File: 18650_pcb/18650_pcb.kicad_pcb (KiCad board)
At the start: 2 copper layers, 40 x 88 mm, 3 parts, among them P1 CONN_01X02

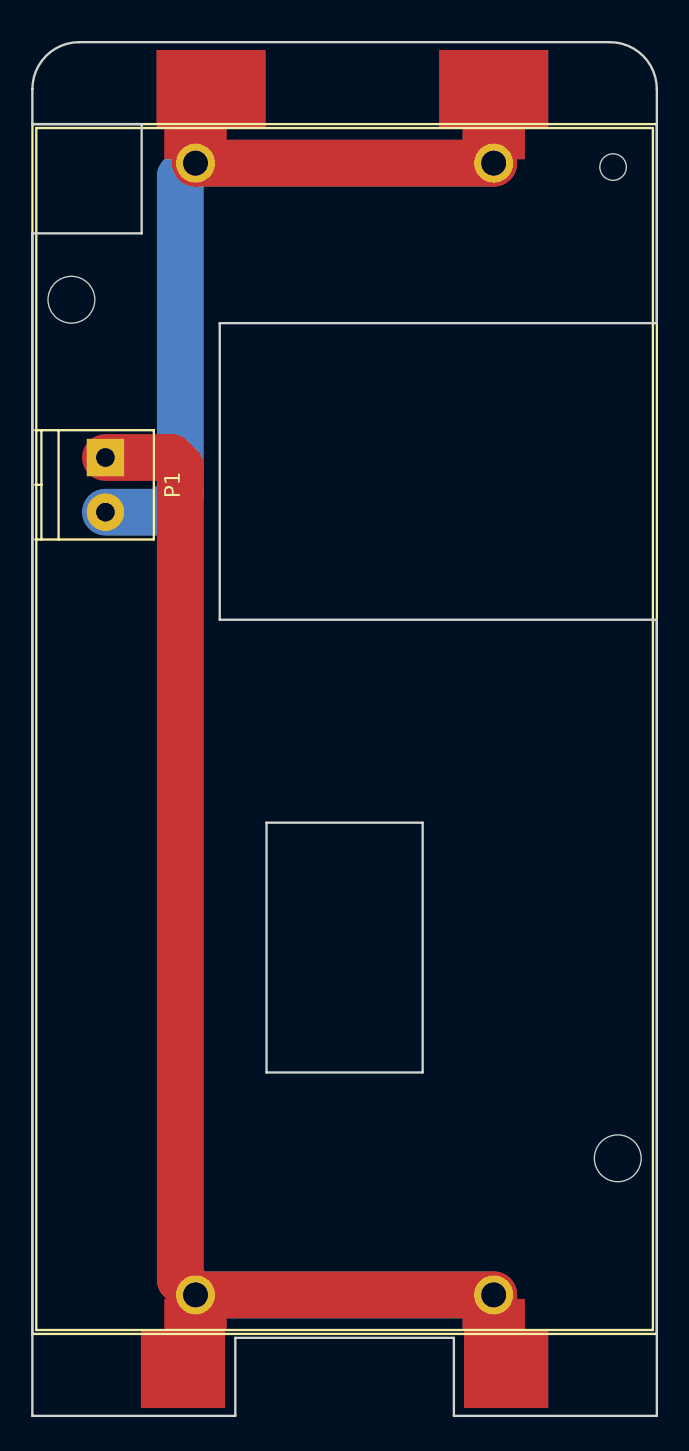
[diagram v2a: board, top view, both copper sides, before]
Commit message: 18650 PCB modifications
-Added version information
-Added a fuse between two batteries
-Added polarity silkscreen markings
-Removed traces from bottom layer to prevent them from shorting out to
metal on back PCB
-Added pads for hand-soldering JST connector wires onto the board
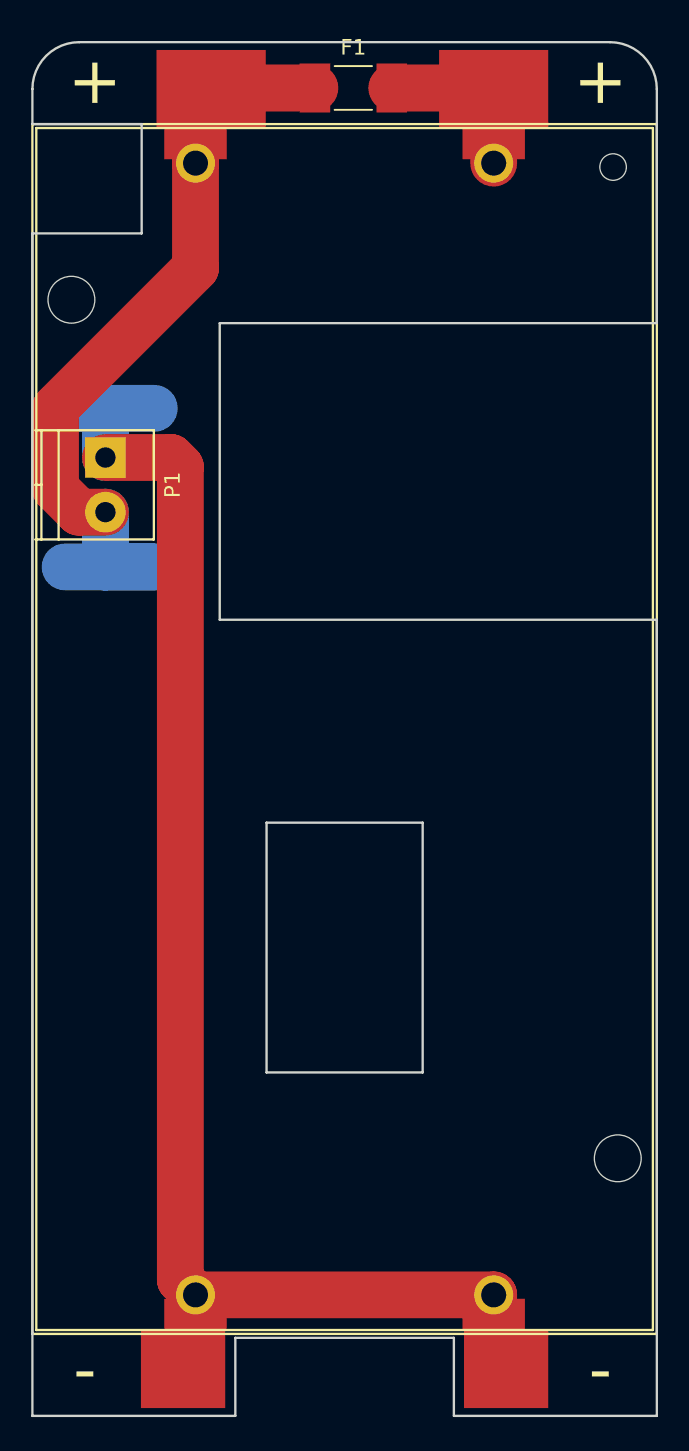
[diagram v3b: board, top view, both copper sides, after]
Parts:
- added F1: 1A, Fuse_Holders_and_Fuses:Fuse_0679H, F.Cu at (150.6, 58.9)
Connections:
- BT1 pad 2: Net-(BT1-Pad1) -> Net-(BT1-Pad2)
- BT2 pad 2: Net-(BT1-Pad1) -> Net-(BT1-Pad2)
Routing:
- net Net-(BT1-Pad1): track 74.7 -> 52.2 mm
- net Net-(BT1-Pad2): track 0.00 -> 11.3 mm
- net Net-(BT1-Pad3): track 106.2 -> 98.5 mm
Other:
- board text added: "+"
- board text added: "-"
- board text added: "18650 PCB ZeroPhone Delta"
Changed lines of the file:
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@@
-(kicad_pcb (version 4) (host pcbnew 4.0.4-stable)
+(kicad_pcb (version 4) (host pcbnew 4.0.6)
   (general
-    (links 12)
-    (no_connects 0)
+    (links 13)
+    (no_connects 2)
     (area 129.924999 55.924999 170.075001 144.075001)
     (thickness 1.6)
-    (drawings 22)
-    (tracks 17)
+    (drawings 28)
+    (tracks 26)
     (zones 0)
-    (modules 3)
-    (nets 3)
+    (modules 4)
+    (nets 4)
   )
   (page A4)
@@
     (mod_text_size 1 1)
     (mod_text_width 0.15)
-    (pad_size 7 5)
-    (pad_drill 0)
+    (pad_size 2.6 2.6)
+    (pad_drill 1.3)
     (pad_to_mask_clearance 0.2)
-    (aux_axis_origin 0 0)
-    (grid_origin 148.57862 104.90804)
-    (visible_elements 7FFFFFFF)
+    (aux_axis_origin 172.09902 54.05724)
+    (grid_origin 172.09902 54.05724)
+    (visible_elements 7FFFFF7F)
     (pcbplotparams
       (layerselection 0x010f0_80000001)
@@
   (net 1 "Net-(BT1-Pad1)")
   (net 2 "Net-(BT1-Pad3)")
+  (net 3 "Net-(BT1-Pad2)")
   (net_class Default "This is the default net class."
     (clearance 0.2)
@@
     (uvia_drill 0.1)
     (add_net "Net-(BT1-Pad1)")
+    (add_net "Net-(BT1-Pad2)")
     (add_net "Net-(BT1-Pad3)")
   )
@@
       (effects (font (size 1 1) (thickness 0.15)))
     )
-    (fp_text value 2x_Battery_Holder (at -0.12138 -27.49196) (layer B.Fab)
+    (fp_text value 2x_Battery_Holder (at -0.12138 -27.49196) (layer B.Fab) hide
       (effects (font (size 1 1) (thickness 0.15)) (justify mirror))
     )
@@
       (net 1 "Net-(BT1-Pad1)"))
     (pad 2 thru_hole circle (at 9.55 -36.25) (size 2.5 2.5) (drill 1.6) (layers *.Cu *.Mask)
-      (net 1 "Net-(BT1-Pad1)"))
+      (net 3 "Net-(BT1-Pad2)"))
     (pad 3 thru_hole circle (at -9.55 36.25) (size 2.5 2.5) (drill 1.6) (layers *.Cu *.Mask)
       (net 2 "Net-(BT1-Pad3)"))
@@
       (effects (font (size 1 1) (thickness 0.15)))
     )
-    (fp_text value 2x_Battery_Holder (at 0.37862 -29.59196 180) (layer F.Fab)
+    (fp_text value 2x_Battery_Holder (at 0.37862 -29.59196) (layer F.Fab) hide
       (effects (font (size 1 1) (thickness 0.15)))
     )
@@
       (net 1 "Net-(BT1-Pad1)"))
     (pad 2 smd rect (at 9.55 -41) (size 7 5) (layers F.Cu F.Paste F.Mask)
-      (net 1 "Net-(BT1-Pad1)"))
+      (net 3 "Net-(BT1-Pad2)"))
     (pad 3 smd rect (at -10.35 41) (size 5.4 5) (layers F.Cu F.Paste F.Mask)
       (net 2 "Net-(BT1-Pad3)"))
@@
       (net 1 "Net-(BT1-Pad1)"))
     (pad 2 smd rect (at 9.55 -37.5) (size 4 2) (layers F.Cu F.Paste F.Mask)
-      (net 1 "Net-(BT1-Pad1)"))
+      (net 3 "Net-(BT1-Pad2)"))
     (pad 3 smd rect (at -9.55 37.5) (size 4 2) (layers F.Cu F.Paste F.Mask)
       (net 2 "Net-(BT1-Pad3)"))
@@
     (fp_line (start 5.25 4.5) (end 5.25 -3.1) (layer F.SilkS) (width 0.15))
     (fp_line (start 5.25 -3.1) (end -1.75 -3.1) (layer F.SilkS) (width 0.15))
-    (pad 2 thru_hole circle (at 3.5 0 270) (size 2.4 2.4) (drill 1.2) (layers *.Cu *.Mask)
-      (net 1 "Net-(BT1-Pad1)"))
-    (pad 1 thru_hole rect (at 0 0 270) (size 2.4 2.4) (drill 1.2) (layers *.Cu *.Mask)
-      (net 2 "Net-(BT1-Pad3)"))
-    (model Terminal_Blocks.3dshapes/TerminalBlock_Pheonix_PT-3.5mm_2pol.wrl
-      (at (xyz 0 0 0))
-      (scale (xyz 1 1 1))
-      (rotate (xyz 0 0 0))
-    )
-  )
+    (pad 2 thru_hole circle (at 3.5 0 270) (size 2.6 2.6) (drill 1.3) (layers *.Cu *.Mask)
+      (net 1 "Net-(BT1-Pad1)"))
+    (pad 1 thru_hole rect (at 0 0 270) (size 2.6 2.6) (drill 1.3) (layers *.Cu *.Mask)
+      (net 2 "Net-(BT1-Pad3)"))
+  )
+  (module Fuse_Holders_and_Fuses:Fuse_0679H (layer F.Cu)
+    (at 150.55982 58.93404)
+    (descr "0679H Series, 2410 Size")
+    (tags Fuse)
+    (attr smd)
+    (fp_text reference F1 (at 0 -2.6) (layer F.SilkS)
+      (effects (font (size 1 1) (thickness 0.15)))
+    )
+    (fp_text value 1A (at 0 2.6) (layer F.Fab)
+      (effects (font (size 1 1) (thickness 0.15)))
+    )
+    (fp_line (start -3.7 1.85) (end -3.7 -1.85) (layer F.CrtYd) (width 0.05))
+    (fp_line (start 3.7 1.85) (end -3.7 1.85) (layer F.CrtYd) (width 0.05))
+    (fp_line (start 3.7 -1.85) (end 3.7 1.85) (layer F.CrtYd) (width 0.05))
+    (fp_line (start -3.7 -1.85) (end 3.7 -1.85) (layer F.CrtYd) (width 0.05))
+    (fp_line (start -1.2 1.4) (end 1.2 1.4) (layer F.SilkS) (width 0.12))
+    (fp_line (start -1.2 -1.4) (end 1.2 -1.4) (layer F.SilkS) (width 0.12))
+    (fp_line (start -3.05 1.27) (end -3.05 -1.27) (layer F.Fab) (width 0.1))
+    (fp_line (start 3.05 1.27) (end -3.05 1.27) (layer F.Fab) (width 0.1))
+    (fp_line (start 3.05 -1.27) (end 3.05 1.27) (layer F.Fab) (width 0.1))
+    (fp_line (start -3.05 -1.27) (end 3.05 -1.27) (layer F.Fab) (width 0.1))
+    (pad 2 smd rect (at 2.46 0) (size 1.96 3.15) (layers F.Cu F.Paste F.Mask)
+      (net 3 "Net-(BT1-Pad2)"))
+    (pad 1 smd rect (at -2.46 0) (size 1.96 3.15) (layers F.Cu F.Paste F.Mask)
+      (net 1 "Net-(BT1-Pad1)"))
+  )
+  (gr_text - (at 166.38402 141.05224) (layer F.SilkS)
+    (effects (font (size 3 3) (thickness 0.6)))
+  )
+  (gr_text - (at 133.36402 141.05224) (layer F.SilkS)
+    (effects (font (size 3 3) (thickness 0.6)))
+  )
+  (gr_text + (at 166.38402 58.50224) (layer F.SilkS)
+    (effects (font (size 3 3) (thickness 0.6)))
+  )
+  (gr_text + (at 133.99902 58.50224) (layer F.SilkS)
+    (effects (font (size 3 3) (thickness 0.6)))
+  )
+  (gr_text "18650 PCB\nZeroPhone Delta" (at 149.87402 68.66224) (layer B.SilkS)
+    (effects (font (size 2 2) (thickness 0.4)) (justify mirror))
+  )
+  (target plus (at 172.09902 54.05724) (size 5) (width 0.15) (layer Edge.Cuts))
   (gr_line (start 137 61.25) (end 130 61.25) (layer Edge.Cuts) (width 0.15))
   (gr_line (start 137 61.25) (end 137 68.25) (layer Edge.Cuts) (width 0.15))
@@
   (gr_line (start 170 74) (end 170 59) (layer Edge.Cuts) (width 0.15))
   (gr_line (start 133 56) (end 167 56) (layer Edge.Cuts) (width 0.15))
-  (segment (start 139.47862 85.00804) (end 139.47862 64.60804) (width 3) (layer B.Cu) (net 1))
-  (segment (start 134.67862 86.10804) (end 138.37862 86.10804) (width 3) (layer B.Cu) (net 1))
-  (segment (start 138.37862 86.10804) (end 139.47862 85.00804) (width 3) (layer B.Cu) (net 1))
-  (segment (start 139.47862 64.60804) (end 140.33666 63.75) (width 3) (layer B.Cu) (net 1))
-  (segment (start 140.33666 63.75) (end 140.45 63.75) (width 3) (layer B.Cu) (net 1))
-  (segment (start 140.45 63.75) (end 159.55 63.75) (width 3) (layer F.Cu) (net 1))
+  (segment (start 137.80902 89.61724) (end 132.09402 89.61724) (width 3) (layer B.Cu) (net 1))
+  (segment (start 134.63402 89.61724) (end 137.80902 89.61724) (width 3) (layer B.Cu) (net 1))
+  (segment (start 134.67862 89.57264) (end 134.63402 89.61724) (width 3) (layer B.Cu) (net 1))
+  (segment (start 134.67862 86.10804) (end 134.67862 89.57264) (width 3) (layer B.Cu) (net 1))
+  (segment (start 148.09982 58.93404) (end 141.51596 58.93404) (width 3) (layer F.Cu) (net 1))
+  (segment (start 141.51596 58.93404) (end 141.45 59) (width 3) (layer F.Cu) (net 1))
+  (segment (start 131.47861 79.43765) (end 140.45 70.46626) (width 3) (layer F.Cu) (net 1))
+  (segment (start 140.45 70.46626) (end 140.45 63.75) (width 3) (layer F.Cu) (net 1))
+  (segment (start 134.67862 86.10804) (end 132.981564 86.10804) (width 3) (layer F.Cu) (net 1))
+  (segment (start 131.47861 84.605086) (end 131.47861 79.43765) (width 3) (layer F.Cu) (net 1))
+  (segment (start 132.981564 86.10804) (end 131.47861 84.605086) (width 3) (layer F.Cu) (net 1))
   (segment (start 140.45 59) (end 140.45 63.75) (width 3) (layer F.Cu) (net 1))
-  (segment (start 159.55 59) (end 159.55 63.75) (width 3) (layer F.Cu) (net 1))
-  (segment (start 140.45 63.75) (end 159.55 63.75) (width 3) (layer B.Cu) (net 1))
+  (segment (start 132.09402 79.45724) (end 137.80902 79.45724) (width 3) (layer B.Cu) (net 2))
+  (segment (start 134.63402 79.45724) (end 132.09402 79.45724) (width 3) (layer B.Cu) (net 2))
+  (segment (start 134.67862 79.50184) (end 134.63402 79.45724) (width 3) (layer B.Cu) (net 2))
+  (segment (start 134.67862 82.60804) (end 134.67862 79.50184) (width 3) (layer B.Cu) (net 2))
+  (segment (start 140.45 136.25) (end 159.55 136.25) (width 3) (layer F.Cu) (net 2))
   (segment (start 134.67862 82.60804) (end 138.87862 82.60804) (width 3) (layer F.Cu) (net 2))
   (segment (start 138.87862 82.60804) (end 139.47862 83.20804) (width 3) (layer F.Cu) (net 2))
   (segment (start 139.47862 83.20804) (end 139.47862 135.27862) (width 3) (layer F.Cu) (net 2))
   (segment (start 139.47862 135.27862) (end 140.45 136.25) (width 3) (layer F.Cu) (net 2))
-  (segment (start 159.55 136.25) (end 140.45 136.25) (width 3) (layer B.Cu) (net 2))
   (segment (start 159.55 136.25) (end 159.55 141) (width 3) (layer F.Cu) (net 2))
-  (segment (start 140.45 136.25) (end 159.55 136.25) (width 3) (layer F.Cu) (net 2))
   (segment (start 140.45 141) (end 140.45 136.25) (width 3) (layer F.Cu) (net 2))
+  (segment (start 153.01982 58.93404) (end 159.48404 58.93404) (width 3) (layer F.Cu) (net 3))
+  (segment (start 159.48404 58.93404) (end 159.55 59) (width 3) (layer F.Cu) (net 3))
+  (segment (start 159.55 59) (end 159.55 63.75) (width 3) (layer F.Cu) (net 3))
+  (zone (net 0) (net_name "") (layer B.Mask) (hatch edge 0.508)
+    (connect_pads (clearance 0.508))
+    (min_thickness 0.254)
+    (fill yes (arc_segments 16) (thermal_gap 0.508) (thermal_bridge_width 0.508))
+    (polygon
+      (pts
+        (xy 130.18902 77.55224) (xy 140.34902 77.55224) (xy 140.34902 81.36224) (xy 130.18902 81.36224)
+      )
+    )
+  )
+  (zone (net 0) (net_name "") (layer B.Mask) (hatch edge 0.508)
+    (connect_pads (clearance 0.508))
+    (min_thickness 0.254)
+    (fill yes (arc_segments 16) (thermal_gap 0.508) (thermal_bridge_width 0.508))
+    (polygon
+      (pts
+        (xy 130.18902 87.71224) (xy 140.34902 87.71224) (xy 140.34902 91.52224) (xy 130.18902 91.52224)
+      )
+    )
+  )
 )

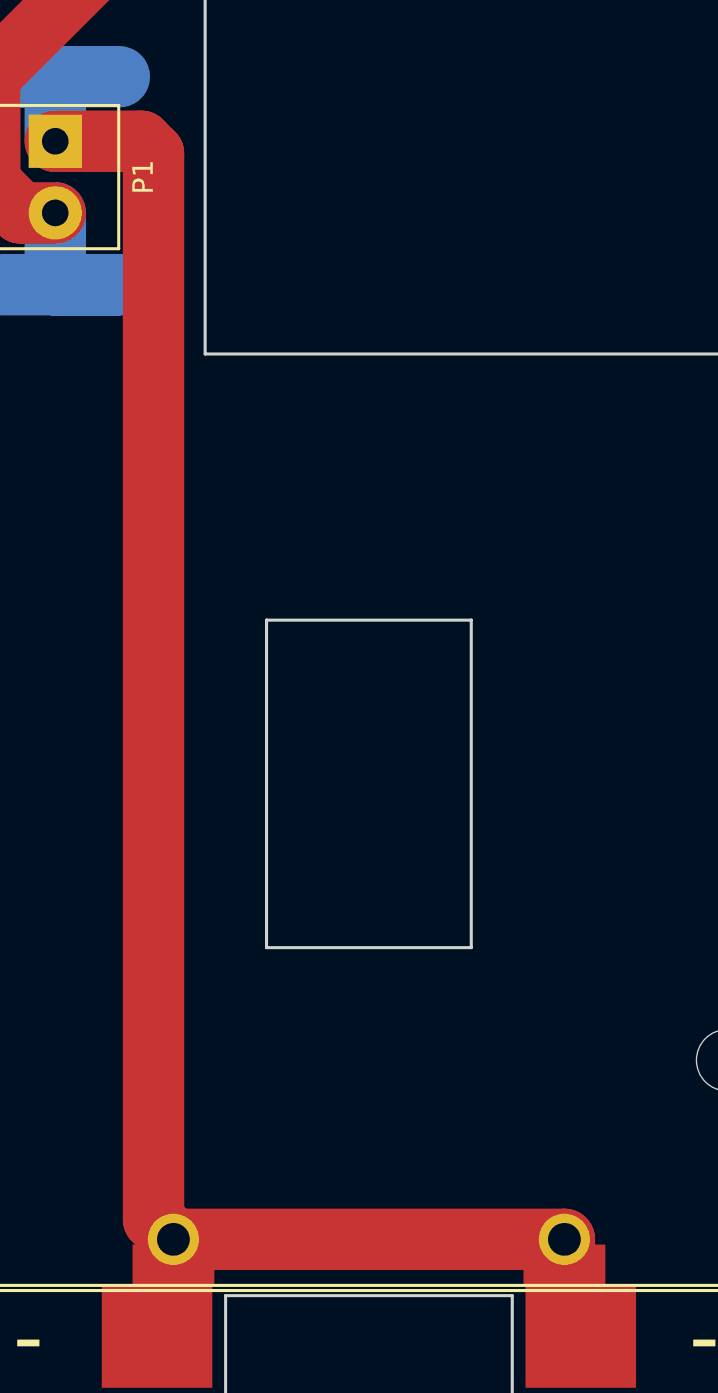
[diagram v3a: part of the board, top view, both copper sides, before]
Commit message: More 18650 board modifications
-Added helper texts
-Moved one trace further from outline
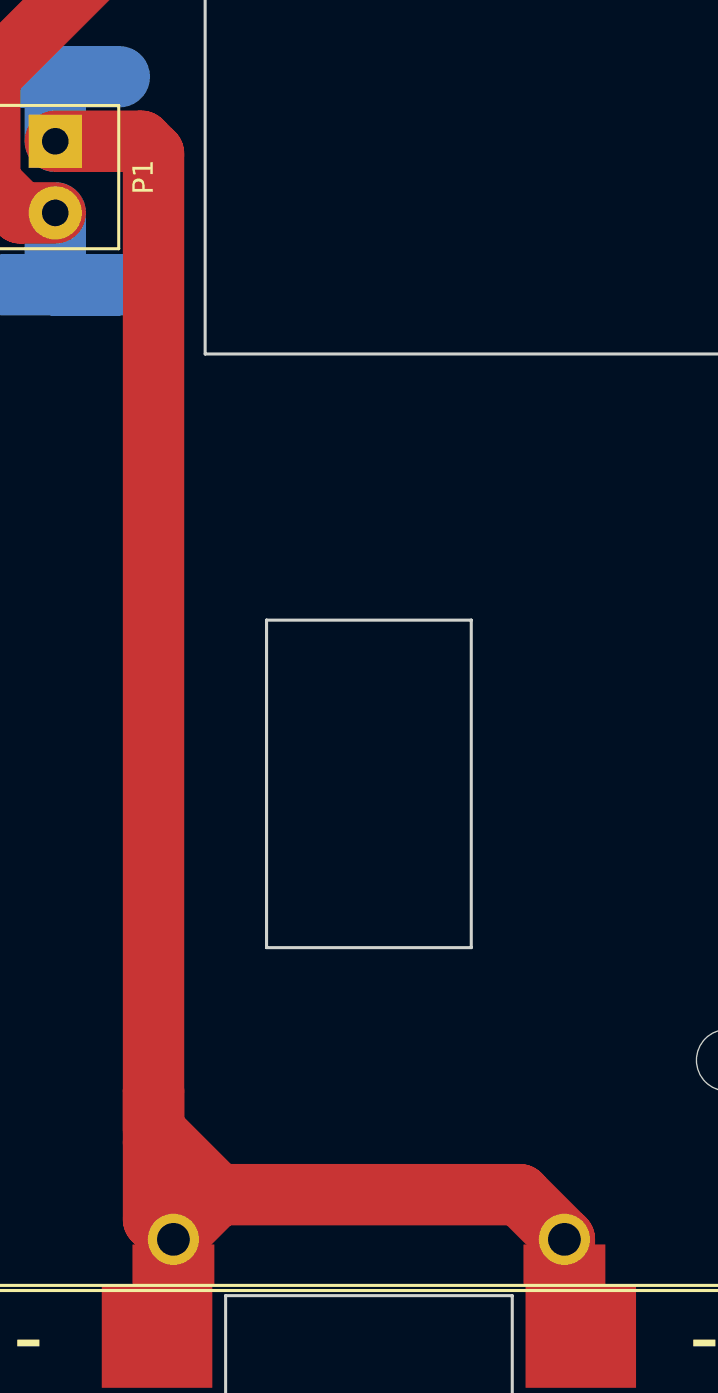
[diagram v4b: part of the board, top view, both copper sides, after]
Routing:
- net Net-(BT1-Pad3): track 98.5 -> 110.9 mm
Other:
- board text added: "1. Remove microSD and nanoSIM cards 2. Insert first battery, charge it fully through microUSB (blue light = full charge) 3. Remove first battery 4. Insert second battery, charge fully 5. Insert first battery"
- board text added: "6. Insert microSD and nanoSIM cards 7. Plug charger in, the green LED should flash in 20 seconds or less"
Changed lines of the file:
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@@
   (general
     (links 13)
-    (no_connects 2)
+    (no_connects 0)
     (area 129.924999 55.924999 170.075001 144.075001)
     (thickness 1.6)
-    (drawings 28)
-    (tracks 26)
+    (drawings 30)
+    (tracks 34)
     (zones 0)
     (modules 4)
@@
       (net 1 "Net-(BT1-Pad1)"))
   )
+  (gr_text "6. Insert microSD and nanoSIM cards\n7. Plug charger in, the green LED \nshould flash in 20 seconds or less" (at 149.23902 126.19324) (layer B.SilkS)
+    (effects (font (size 1 1) (thickness 0.25)) (justify mirror))
+  )
+  (gr_text "1. Remove microSD and nanoSIM cards\n2. Insert first battery, charge it fully\nthrough microUSB (blue light = full charge)\n3. Remove first battery\n4. Insert second battery, charge fully\n5. Insert first battery" (at 149.74702 99.26924) (layer B.SilkS)
+    (effects (font (size 1 1) (thickness 0.25)) (justify mirror))
+  )
   (gr_text - (at 166.38402 141.05224) (layer F.SilkS)
     (effects (font (size 3 3) (thickness 0.6)))
@@
     (effects (font (size 3 3) (thickness 0.6)))
   )
-  (gr_text "18650 PCB\nZeroPhone Delta" (at 149.87402 68.66224) (layer B.SilkS)
+  (gr_text "18650 PCB\nZeroPhone Delta" (at 149.74702 69.29724) (layer B.SilkS)
     (effects (font (size 2 2) (thickness 0.4)) (justify mirror))
   )
@@
   (segment (start 132.981564 86.10804) (end 131.47861 84.605086) (width 3) (layer F.Cu) (net 1))
   (segment (start 140.45 59) (end 140.45 63.75) (width 3) (layer F.Cu) (net 1))
+  (segment (start 139.47862 128.98724) (end 139.47862 131.52724) (width 3) (layer F.Cu) (net 2))
+  (segment (start 139.47862 128.98724) (end 139.47862 130.9131) (width 3) (layer F.Cu) (net 2))
+  (segment (start 139.47862 83.20804) (end 139.47862 128.98724) (width 3) (layer F.Cu) (net 2))
+  (segment (start 139.47862 130.9131) (end 142.63276 134.06724) (width 3) (layer F.Cu) (net 2))
+  (segment (start 139.47862 131.52724) (end 139.47862 135.27862) (width 3) (layer F.Cu) (net 2))
+  (segment (start 142.63276 134.06724) (end 142.01862 134.06724) (width 3) (layer F.Cu) (net 2))
+  (segment (start 142.01862 134.06724) (end 139.47862 131.52724) (width 3) (layer F.Cu) (net 2))
+  (segment (start 159.55 136.25) (end 157.36724 134.06724) (width 3) (layer F.Cu) (net 2))
+  (segment (start 142.63276 134.06724) (end 157.36724 134.06724) (width 3) (layer F.Cu) (net 2))
+  (segment (start 140.45 136.25) (end 142.63276 134.06724) (width 3) (layer F.Cu) (net 2))
   (segment (start 132.09402 79.45724) (end 137.80902 79.45724) (width 3) (layer B.Cu) (net 2))
   (segment (start 134.63402 79.45724) (end 132.09402 79.45724) (width 3) (layer B.Cu) (net 2))
   (segment (start 134.67862 79.50184) (end 134.63402 79.45724) (width 3) (layer B.Cu) (net 2))
   (segment (start 134.67862 82.60804) (end 134.67862 79.50184) (width 3) (layer B.Cu) (net 2))
-  (segment (start 140.45 136.25) (end 159.55 136.25) (width 3) (layer F.Cu) (net 2))
   (segment (start 134.67862 82.60804) (end 138.87862 82.60804) (width 3) (layer F.Cu) (net 2))
   (segment (start 138.87862 82.60804) (end 139.47862 83.20804) (width 3) (layer F.Cu) (net 2))
-  (segment (start 139.47862 83.20804) (end 139.47862 135.27862) (width 3) (layer F.Cu) (net 2))
   (segment (start 139.47862 135.27862) (end 140.45 136.25) (width 3) (layer F.Cu) (net 2))
   (segment (start 159.55 136.25) (end 159.55 141) (width 3) (layer F.Cu) (net 2))
